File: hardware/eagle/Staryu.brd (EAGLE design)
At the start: 52.1 x 34.9 mm, 37 parts, among them IC1 ATMEGA32U2-QFN, J1 MYCON2_USB-MINI-B, J3 AVR_ISP, SW1 CHERRY-MX-LED-MOD, SW1-2 CHERRY-MX-LED-MOD, SW2 CHERRY-MX-LED-MOD, SW2-2 CHERRY-MX-LED-MOD, SW3 CHERRY-MX-LED-MOD, SW3-2 CHERRY-MX-LED-MOD, SW4 CHERRY-MX-LED-MOD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

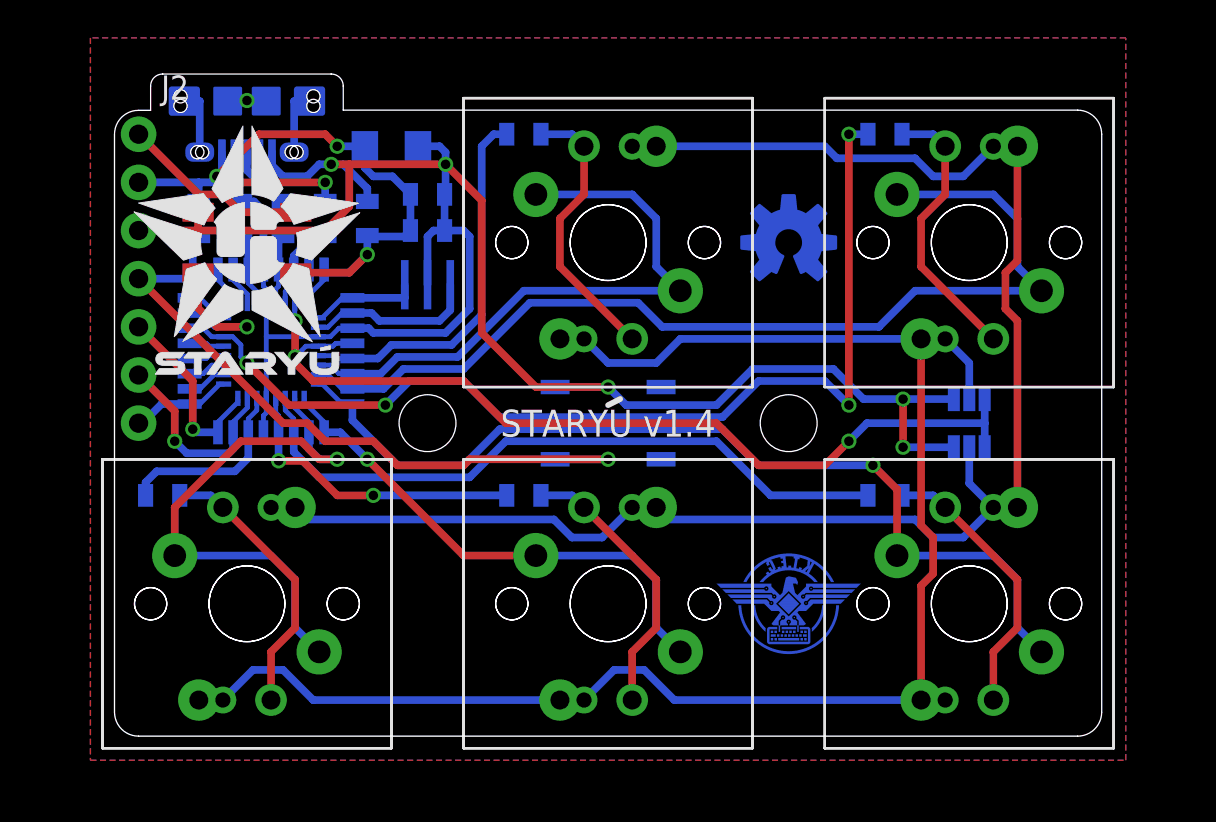
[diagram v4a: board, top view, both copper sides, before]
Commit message: Update hardware to v1.5 - Improve jumpers for selecting switch mounting - Change logo
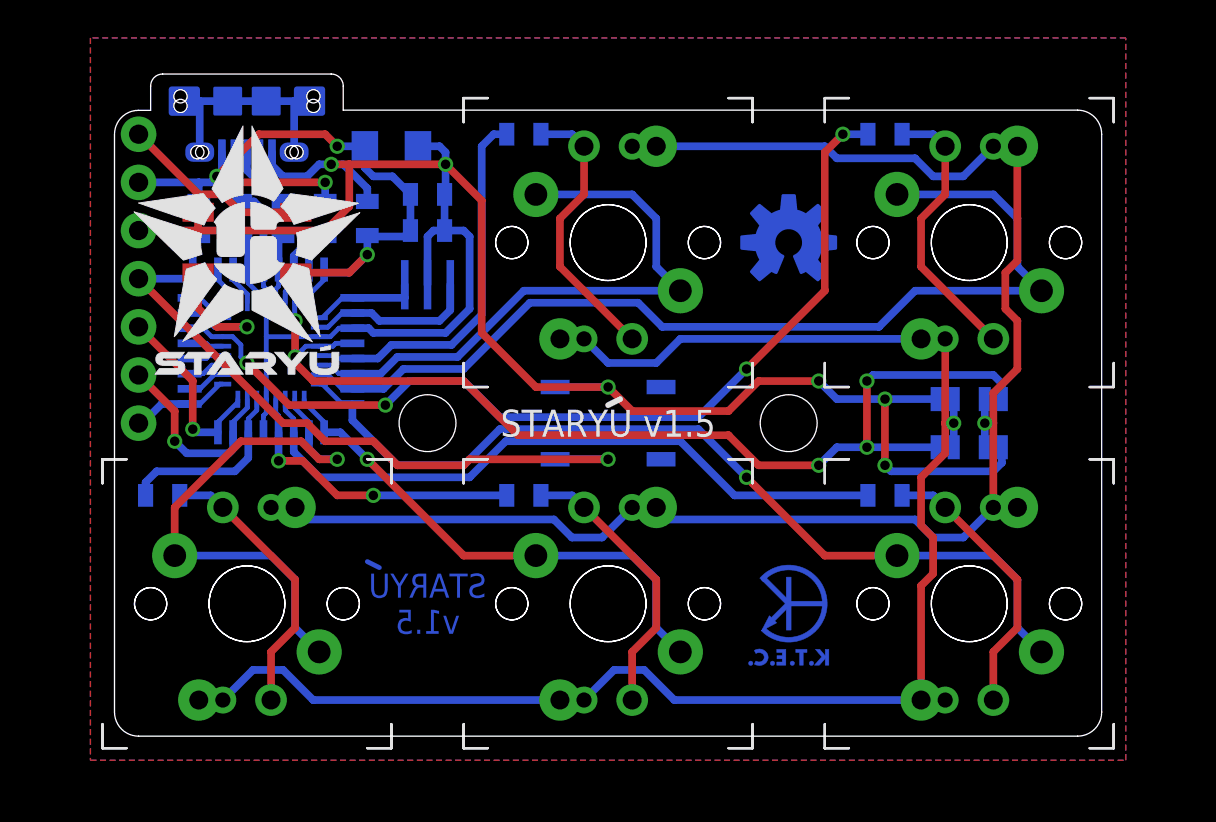
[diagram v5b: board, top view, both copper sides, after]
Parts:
- removed IC1: ATMEGA32U2-QFN, atmega32u2:QFN32
- removed JP1, JP2: JUMPER-PAD-3-2OF3_NC_BY_PASTE, SparkFun-Passives:PAD-JUMPER-3-2OF3_NC_BY_PASTE_YES_SILK_FULL_BOX
- removed U$1: K.T.E.C._LOGO.3_INCH_EXP, logo:K.T.E.C._LOGO_COPPER_EXPOSED_.3
- added JP3, JP4, JP5, JP6: JUMPER-PAD-2-NO, SparkFun-Passives:PAD-JUMPER-2-NO_NO_SILK
- added LOGO2: STARYU_LOGO, Noukensha:STARYU_LOGO
- added U1-2: ATMEGA32U2-QFN_MOD, atmega32u2:QFN32_MOD
- LOGO1: value STARYU_LOGO -> K.T.E.C._LOGO3_COPPER_EXP_S; device Noukensha:STARYU_LOGO -> logo:K.T.E.C._LOGO3_COPPER_EXPOSED_S
- U1: value ATMEGA32U2-TQFP -> ATMEGA32U2-TQFP_MOD; device atmega32u2:TQFP32-08 -> atmega32u2:TQFP32-08_MOD
- moved LOGO1 34.3 mm to (38.1, 9.53), flipped to the bottom
- renumbered U$3 to LOGO4
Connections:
- removed net JP1: JP1.2, SW1-2.SW2, SW1.LED1, SW2-2.SW2, SW2.LED1, SW3-2.SW2, SW3.LED1, SW4-2.SW2, SW4.LED1, SW5-2.SW2, SW5.LED1
- removed net JP2: JP2.2, SW1-2.LED1, SW1.SW2, SW2-2.LED1, SW2.SW2, SW3-2.LED1, SW3.SW2, SW4-2.LED1, SW4.SW2, SW5-2.LED1, SW5.SW2
- new net JP3-4: JP3.1, JP4.2, SW1-2.SW2, SW1.LED1, SW2-2.SW2, SW2.LED1, SW3-2.SW2, SW3.LED1, SW4-2.SW2, SW4.LED1, SW5-2.SW2, SW5.LED1
- new net JP5-6: JP5.1, JP6.2, SW1-2.LED1, SW1.SW2, SW2-2.LED1, SW2.SW2, SW3-2.LED1, SW3.SW2, SW4-2.LED1, SW4.SW2, SW5-2.LED1, SW5.SW2
- net 5V: now also JP3.2, JP5.2, U1-2.31, U1-2.32, U1-2.4; no longer IC1.31, IC1.32, IC1.4, JP1.1, JP2.3
- net GND: now also JP4.1, JP6.1, U1-2.13, U1-2.28, U1-2.3; no longer IC1.13, IC1.28, IC1.3, JP1.3, JP2.1
- net LED1: now also U1-2.5; no longer IC1.5
- net LED2: now also U1-2.22; no longer IC1.22
- net LED3: now also U1-2.11; no longer IC1.11
- net LED4: now also U1-2.12; no longer IC1.12
- net LED5: now also U1-2.14; no longer IC1.14
- net MISO: now also U1-2.17; no longer IC1.17
- net MOSI: now also U1-2.16; no longer IC1.16
- net N$1: now also U1-2.29; no longer IC1.29
- net N$2: now also U1-2.30; no longer IC1.30
- net N$20: now also U1-2.18; no longer IC1.18
- net N$21: now also U1-2.19; no longer IC1.19
- net N$22: now also U1-2.20; no longer IC1.20
- net N$23: now also U1-2.21; no longer IC1.21
- net N$24: now also U1-2.26; no longer IC1.26
- net N$25: now also U1-2.25; no longer IC1.25
- net N$5: now also U1-2.1; no longer IC1.1
- net N$6: now also U1-2.2; no longer IC1.2
- net N$7: now also U1-2.27; no longer IC1.27
- net N$8: now also U1-2.24; no longer IC1.24
- net RGB: now also U1-2.23; no longer IC1.23
- net SCK: now also U1-2.15; no longer IC1.15
- net SW1: now also U1-2.6; no longer IC1.6
- net SW2: now also U1-2.7; no longer IC1.7
- net SW3: now also U1-2.8; no longer IC1.8
- net SW4: now also U1-2.9; no longer IC1.9
- net SW5: now also U1-2.10; no longer IC1.10
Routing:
- net JP2: track 86.9 -> 0.00 mm
- net JP5-6: track 0.00 -> 86.7 mm, vias 0 -> 1
- net JP1: track 86.6 -> 0.00 mm
- net JP3-4: track 0.00 -> 86.5 mm, vias 0 -> 1
- net 5V: track 85.7 -> 91.8 mm, vias 6 -> 8
- net SHIELD: track 7.01 -> 12.8 mm, vias 1 -> 0
- net LED2: track 54.7 -> 49.6 mm
- net GND: track 113.4 -> 117.8 mm, vias 5 -> 6
- net SW3: track 49.6 -> 47.5 mm
- net N$14: track 0.00 -> 0.71 mm
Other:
- board text added: "JP1"
- board text added: "JP2"
- board text added: "STARYU v1.5"
- board text removed: "N"
- board text removed: "R"
- board text removed: "STARYU v1.4"

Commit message: Update hardware to v1.6 - Optimize routing under ATMEGA32U2-MU to avoid short by thermal pad
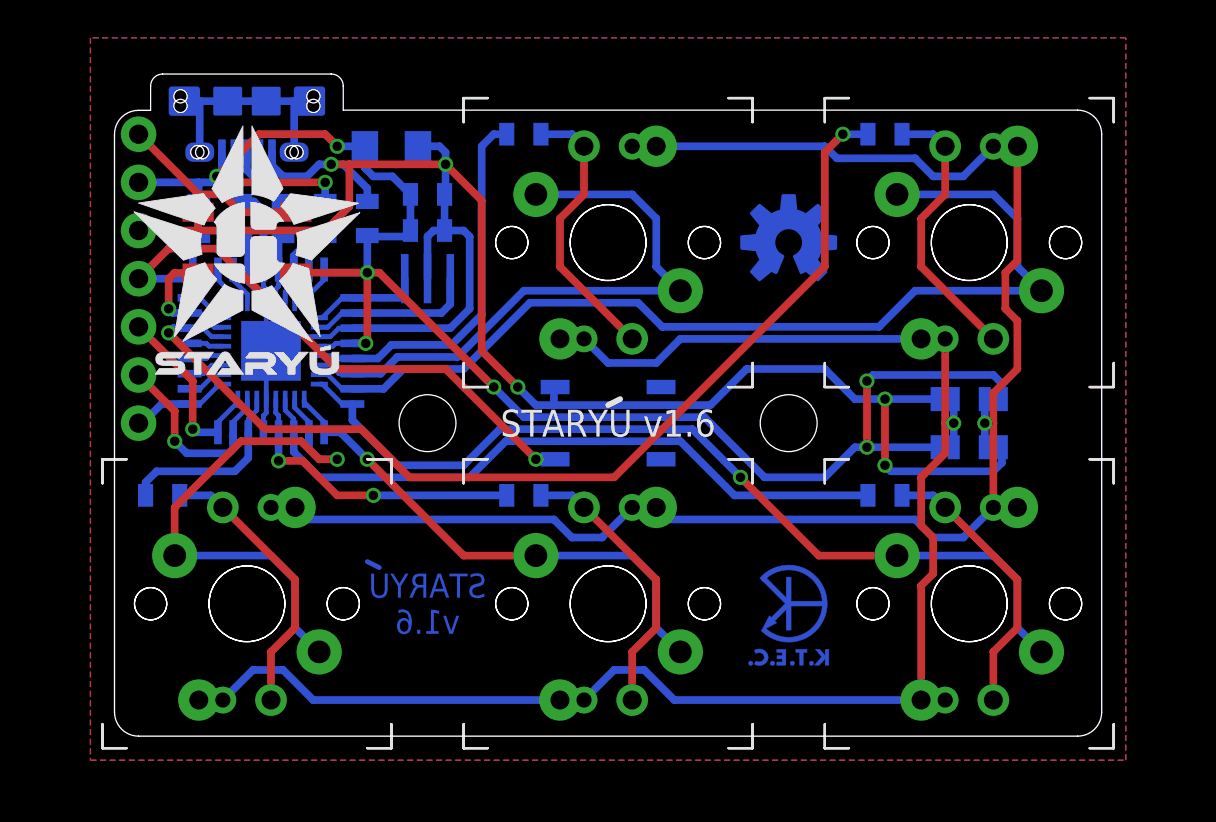
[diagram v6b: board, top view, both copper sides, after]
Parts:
- moved Y1 0.32 mm to (19.1, 26.7)
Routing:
- net LED2: track 49.6 -> 54.2 mm, vias 4 -> 2
- net N$8: track 40.3 -> 35.8 mm
- net RGB: track 8.18 -> 6.51 mm
- net GND: track 117.8 -> 116.3 mm, vias 6 -> 5
- net 5V: track 91.8 -> 90.4 mm, vias 8 -> 7
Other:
- board text added: "STARYU v1.6"
- board text removed: "STARYU v1.5"
